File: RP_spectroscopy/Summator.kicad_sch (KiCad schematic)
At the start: 18 parts, among them U1 AD8603, U2 ADG417BR

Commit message: Almost finished the summator. Added also some components in the connectors schematic
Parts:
- added C7: 2.2µ, symbol Device:C
- added R11: 47R, symbol Device:R
- added R12, R13, R14, R15, R16, R17: 3k, symbol Device:R
- added R18: 49R9, symbol Device:R
- added R19: 1k, symbol Device:R
- added RV1: 20k, symbol Device:R_Potentiometer_Trim
- added TP1: TestPoint_Flag, symbol Connector:TestPoint_Flag
- added U3: AD8397, Package_CSP:LFCSP-8-1EP_3x3mm_P0.5mm_EP1.6x2.34mm, symbol Amplifier_Operational:ADA4610-2xCP
- C1, C2, C3, C4, C5, C6: value C -> 2.2µ
- R10: value R -> 20k
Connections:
- net GND: now also U1.2 (V-), U2.3 (GND), C7.2, R11.2, RV1.1, U3.5 (+)
- net Sweep/Fast PID: now also R11.1, R12.1, R13.1
- net at U2.8: now also R12.2, U3.3 (+)
- net at R10.2, U1.1: now also R16.1
- net at U1.3 (+): now also RV1.2, TP1.1
- net +3V3: now reaches U1.5 (V+)
- net +3V3: now also R19.1
- net +5VA: now reaches U2.4 (V+)
- net +5VA: now also U3.8 (V+)
- net -5VA: now reaches U2.7 (V-)
- net -5VA: now also U3.4 (V-), U3.9 (V-)
- new net: R13.2, R14.1, U3.2 (-)
- new net: R14.2, R15.1, U3.1
- new net: R15.2, R16.2, R17.1, U3.6 (-)
- new net: R17.2, R18.1, U3.7
- new net: C7.1, R19.2, RV1.3
- new net Summed signals: R18.2
- no-connect marks 0 -> 1
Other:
- moved on the sheet: R10

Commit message: Continued with the connection scheet
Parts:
- U1: footprint Package_TO_SOT_SMD:TSOT-23-5 -> Package_TO_SOT_SMD:TSOT-23-5_HandSoldering
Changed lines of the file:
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@@
 			)
 		)
-		(property "Footprint" "Package_TO_SOT_SMD:TSOT-23-5"
+		(property "Footprint" "Package_TO_SOT_SMD:TSOT-23-5_HandSoldering"
 			(at 160.02 128.27 0)
 			(effects

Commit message: Commit before deleting the VCO schematic from the main project. I have a separate project for that.
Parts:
- C1, C2, C3, C4, C5, C6, C7: footprint (none) -> Capacitor_SMD:C_0805_2012Metric_Pad1.18x1.45mm_HandSolder
- R1, R10, R11, R12, R13, R14, R15, R16, R17, R18, R19, R2, R3, R4, R5, R6, R7, R8, R9: footprint (none) -> Resistor_SMD:R_0805_2012Metric_Pad1.20x1.40mm_HandSolder
- RV1: footprint (none) -> Potentiometer_SMD:Potentiometer_Bourns_3224G_Horizontal
- TP1: footprint (none) -> TestPoint:TestPoint_Pad_3.0x3.0mm
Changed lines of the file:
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@@
 			)
 		)
-		(property "Footprint" ""
+		(property "Footprint" "Resistor_SMD:R_0805_2012Metric_Pad1.20x1.40mm_HandSolder"
 			(at 53.34 90.932 90)
 			(effects
@@
 			)
 		)
-		(property "Description" "Resistor"
+		(property "Description" "Resistor, 1k 1%"
 			(at 53.34 92.71 0)
 			(effects
@@
 			)
 		)
-		(property "Footprint" ""
+		(property "Footprint" "Resistor_SMD:R_0805_2012Metric_Pad1.20x1.40mm_HandSolder"
 			(at 45.212 73.66 90)
 			(effects
@@
 			)
 		)
-		(property "Description" "Resistor"
+		(property "Description" "Resistor, 47R 1%"
 			(at 46.99 73.66 0)
 			(effects
@@
 			)
 		)
-		(property "Footprint" ""
+		(property "Footprint" "Resistor_SMD:R_0805_2012Metric_Pad1.20x1.40mm_HandSolder"
 			(at 53.34 167.132 90)
 			(effects
@@
 			)
 		)
-		(property "Description" "Resistor"
+		(property "Description" "Resistor, 1k 1%"
 			(at 53.34 168.91 0)
 			(effects
@@
 			)
 		)
-		(property "Footprint" ""
+		(property "Footprint" "Resistor_SMD:R_0805_2012Metric_Pad1.20x1.40mm_HandSolder"
 			(at 53.34 129.032 90)
 			(effects
@@
 			)
 		)
-		(property "Description" "Resistor"
+		(property "Description" "Resistor, 1k 1%"
 			(at 53.34 130.81 0)
 			(effects
@@
 			)
 		)
-		(property "Footprint" ""
+		(property "Footprint" "Resistor_SMD:R_0805_2012Metric_Pad1.20x1.40mm_HandSolder"
 			(at 68.58 75.438 90)
 			(effects
@@
 			)
 		)
-		(property "Description" "Resistor"
+		(property "Description" "Resistor, 3k 1%"
 			(at 68.58 73.66 0)
 			(effects
@@
 			)
 		)
-		(property "Footprint" ""
+		(property "Footprint" "Capacitor_SMD:C_0805_2012Metric_Pad1.18x1.45mm_HandSolder"
 			(at 100.0252 106.68 0)
 			(effects
@@
 			)
 		)
-		(property "Description" "Unpolarized capacitor"
+		(property "Description" "Unpolarized capacitor, 2.2µ X7R 50V"
 			(at 99.06 102.87 0)
 			(effects
@@
 			)
 		)
-		(property "Footprint" ""
+		(property "Footprint" "Resistor_SMD:R_0805_2012Metric_Pad1.20x1.40mm_HandSolder"
 			(at 85.09 83.058 90)
 			(effects
@@
 			)
 		)
-		(property "Description" "Resistor"
+		(property "Description" "Resistor, 3k 1%"
 			(at 85.09 81.28 0)
 			(effects
@@
 			)
 		)
-		(property "Footprint" ""
+		(property "Footprint" "Resistor_SMD:R_0805_2012Metric_Pad1.20x1.40mm_HandSolder"
 			(at 83.82 167.132 90)
 			(effects
@@
 			)
 		)
-		(property "Description" "Resistor"
+		(property "Description" "Resistor, 1k 1%"
 			(at 83.82 168.91 0)
 			(effects
@@
 			)
 		)
-		(property "Footprint" ""
+		(property "Footprint" "Resistor_SMD:R_0805_2012Metric_Pad1.20x1.40mm_HandSolder"
 			(at 127 145.288 90)
 			(effects
@@
 			)
 		)
-		(property "Footprint" ""
+		(property "Footprint" "Resistor_SMD:R_0805_2012Metric_Pad1.20x1.40mm_HandSolder"
 			(at 127 119.888 90)
 			(effects
@@
 			)
 		)
-		(property "Footprint" ""
+		(property "Footprint" "Capacitor_SMD:C_0805_2012Metric_Pad1.18x1.45mm_HandSolder"
 			(at 69.5452 106.68 0)
 			(effects
@@
 			)
 		)
-		(property "Description" "Unpolarized capacitor"
+		(property "Description" "Unpolarized capacitor, 2.2µ X7R 50V"
 			(at 68.58 102.87 0)
 			(effects
@@
 			)
 		)
-		(property "Footprint" ""
+		(property "Footprint" "Resistor_SMD:R_0805_2012Metric_Pad1.20x1.40mm_HandSolder"
 			(at 83.82 90.932 90)
 			(effects
@@
 			)
 		)
-		(property "Description" "Resistor"
+		(property "Description" "Resistor, 1k 1%"
 			(at 83.82 92.71 0)
 			(effects
@@
 			)
 		)
-		(property "Footprint" ""
+		(property "Footprint" "Resistor_SMD:R_0805_2012Metric_Pad1.20x1.40mm_HandSolder"
 			(at 160.02 152.908 90)
 			(effects
@@
 			)
 		)
-		(property "Description" "Resistor"
+		(property "Description" "Resistor, 20k 1%"
 			(at 160.02 151.13 0)
 			(effects
@@
 			)
 		)
-		(property "Footprint" ""
+		(property "Footprint" "Resistor_SMD:R_0805_2012Metric_Pad1.20x1.40mm_HandSolder"
 			(at 68.58 62.738 90)
 			(effects
@@
 			)
 		)
-		(property "Description" "Resistor"
+		(property "Description" "Resistor, 3k 1%"
 			(at 68.58 60.96 0)
 			(effects
@@
 			)
 		)
-		(property "Footprint" ""
+		(property "Footprint" "Capacitor_SMD:C_0805_2012Metric_Pad1.18x1.45mm_HandSolder"
 			(at 69.5452 144.78 0)
 			(effects
@@
 			)
 		)
-		(property "Description" "Unpolarized capacitor"
+		(property "Description" "Unpolarized capacitor, 2.2µ X7R 50V"
 			(at 68.58 140.97 0)
 			(effects
@@
 			)
 		)
-		(property "Footprint" ""
+		(property "Footprint" "Capacitor_SMD:C_0805_2012Metric_Pad1.18x1.45mm_HandSolder"
 			(at 100.0252 144.78 0)
 			(effects
@@
 			)
 		)
-		(property "Description" "Unpolarized capacitor"
+		(property "Description" "Unpolarized capacitor, 2.2µ X7R 50V"
 			(at 99.06 140.97 0)
 			(effects
@@
 			)
 		)
-		(property "Footprint" ""
+		(property "Footprint" "Resistor_SMD:R_0805_2012Metric_Pad1.20x1.40mm_HandSolder"
 			(at 187.96 102.108 90)
 			(effects
@@
 			)
 		)
-		(property "Description" "Resistor"
+		(property "Description" "Resistor, 3k 1%"
 			(at 187.96 100.33 0)
 			(effects
@@
 			)
 		)
-		(property "Footprint" ""
+		(property "Footprint" "Resistor_SMD:R_0805_2012Metric_Pad1.20x1.40mm_HandSolder"
 			(at 127 132.588 90)
 			(effects
@@
 			)
 		)
-		(property "Footprint" ""
+		(property "Footprint" "Resistor_SMD:R_0805_2012Metric_Pad1.20x1.40mm_HandSolder"
 			(at 233.68 93.218 90)
 			(effects
@@
 			)
 		)
-		(property "Description" "Resistor"
+		(property "Description" "Resistor, 49R9 1%"
 			(at 233.68 91.44 0)
 			(effects
@@
 			)
 		)
-		(property "Footprint" ""
+		(property "Footprint" "Capacitor_SMD:C_0805_2012Metric_Pad1.18x1.45mm_HandSolder"
 			(at 69.5452 182.88 0)
 			(effects
@@
 			)
 		)
-		(property "Description" "Unpolarized capacitor"
+		(property "Description" "Unpolarized capacitor, 2.2µ X7R 50V"
 			(at 68.58 179.07 0)
 			(effects
@@
 			)
 		)
-		(property "Footprint" ""
+		(property "Footprint" "Capacitor_SMD:C_0805_2012Metric_Pad1.18x1.45mm_HandSolder"
 			(at 100.0252 182.88 0)
 			(effects
@@
 			)
 		)
-		(property "Description" "Unpolarized capacitor"
+		(property "Description" "Unpolarized capacitor, 2.2µ X7R 50V"
 			(at 99.06 179.07 0)
 			(effects
@@
 			)
 		)
-		(property "Footprint" ""
+		(property "Footprint" "TestPoint:TestPoint_Pad_3.0x3.0mm"
 			(at 135.89 99.06 0)
 			(effects
@@
 			)
 		)
-		(property "Footprint" ""
+		(property "Footprint" "Potentiometer_SMD:Potentiometer_Bourns_3224G_Horizontal"
 			(at 152.4 99.06 0)
 			(effects
@@
 			)
 		)
-		(property "Description" "Trim-potentiometer"
+		(property "Description" "Trim-potentiometer, 20k"
 			(at 152.4 99.06 0)
 			(effects
@@
 			)
 		)
-		(property "Footprint" ""
+		(property "Footprint" "Resistor_SMD:R_0805_2012Metric_Pad1.20x1.40mm_HandSolder"
 			(at 214.63 109.728 90)
 			(effects
@@
 			)
 		)
-		(property "Description" "Resistor"
+		(property "Description" "Resistor, 3k 1%"
 			(at 214.63 107.95 0)
 			(effects
@@
 			)
 		)
-		(property "Footprint" ""
+		(property "Footprint" "Capacitor_SMD:C_0805_2012Metric_Pad1.18x1.45mm_HandSolder"
 			(at 166.0652 102.87 0)
 			(effects
@@
 			)
 		)
-		(property "Description" "Unpolarized capacitor"
+		(property "Description" "Unpolarized capacitor, 2.2µ X7R 50V"
 			(at 165.1 99.06 0)
 			(effects
@@
 			)
 		)
-		(property "Footprint" ""
+		(property "Footprint" "Resistor_SMD:R_0805_2012Metric_Pad1.20x1.40mm_HandSolder"
 			(at 83.82 129.032 90)
 			(effects
@@
 			)
 		)
-		(property "Description" "Resistor"
+		(property "Description" "Resistor, 1k 1%"
 			(at 83.82 130.81 0)
 			(effects
@@
 			)
 		)
-		(property "Footprint" ""
+		(property "Footprint" "Resistor_SMD:R_0805_2012Metric_Pad1.20x1.40mm_HandSolder"
 			(at 150.622 88.9 90)
 			(effects
@@
 			)
 		)
-		(property "Description" "Resistor"
+		(property "Description" "Resistor, 1k 1%"
 			(at 152.4 88.9 0)
 			(effects
@@
 			)
 		)
-		(property "Footprint" ""
+		(property "Footprint" "Resistor_SMD:R_0805_2012Metric_Pad1.20x1.40mm_HandSolder"
 			(at 187.96 89.408 90)
 			(effects
@@
 			)
 		)
-		(property "Description" "Resistor"
+		(property "Description" "Resistor, 3k 1%"
 			(at 187.96 87.63 0)
 			(effects

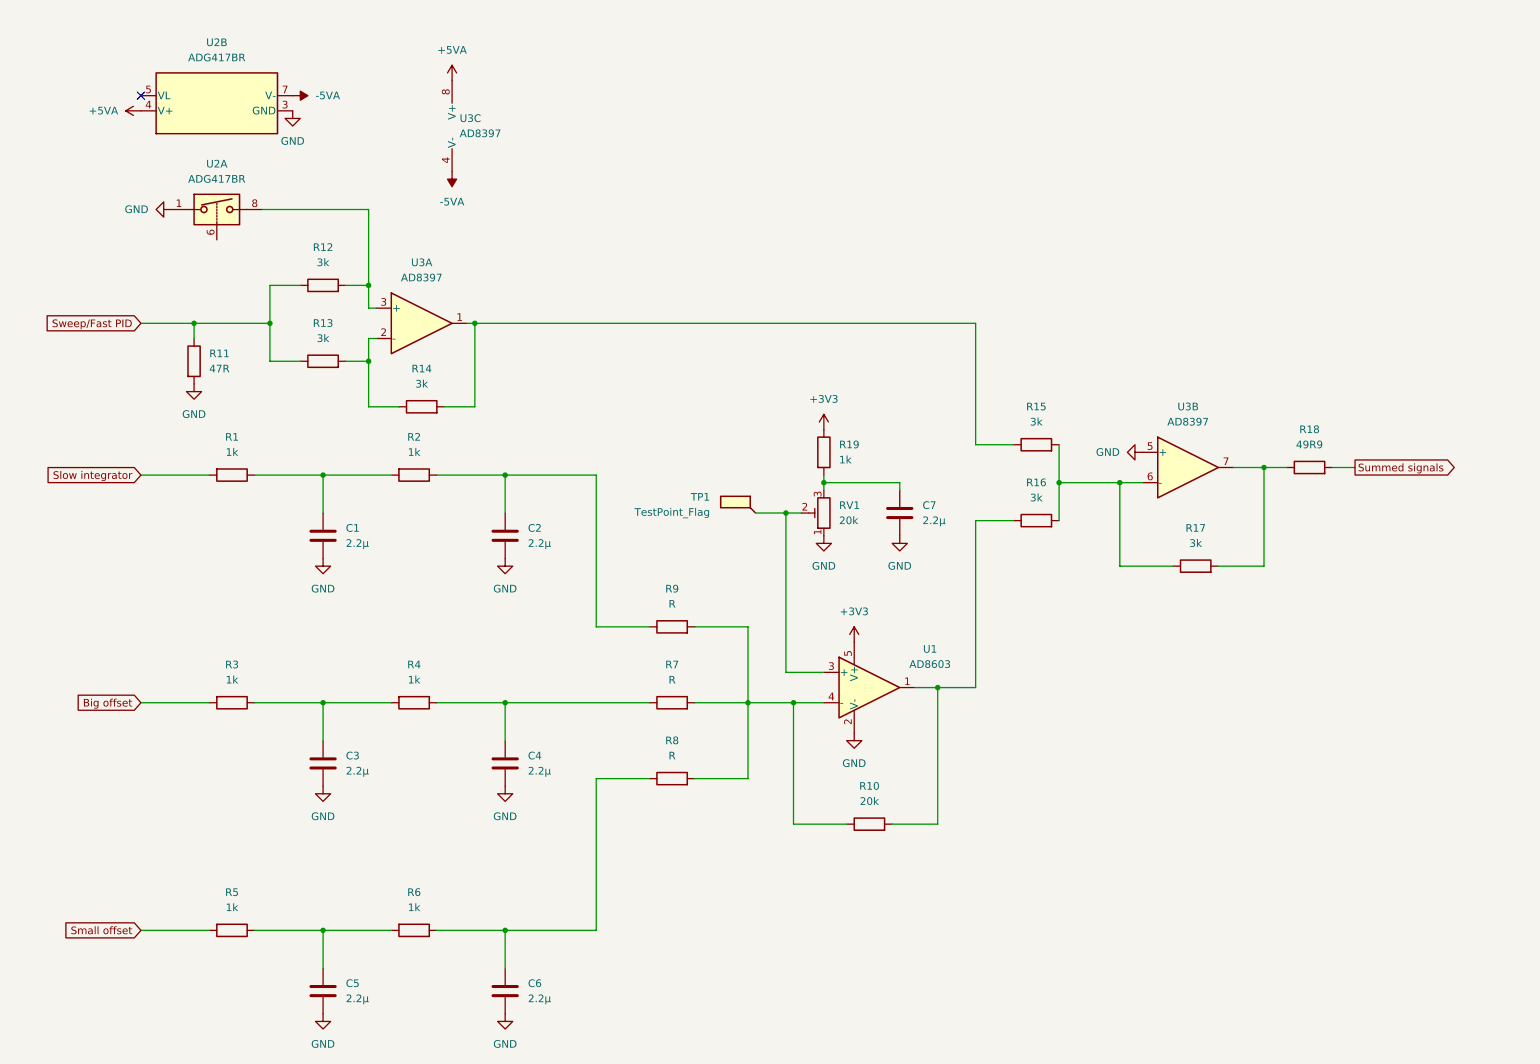
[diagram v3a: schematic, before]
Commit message: Added the EMI filter in the +5V branch and added the powerline capacitors for the remaining opamps. Removed the tunable offset from the summator. Assigned right footprints and specs to all the components.
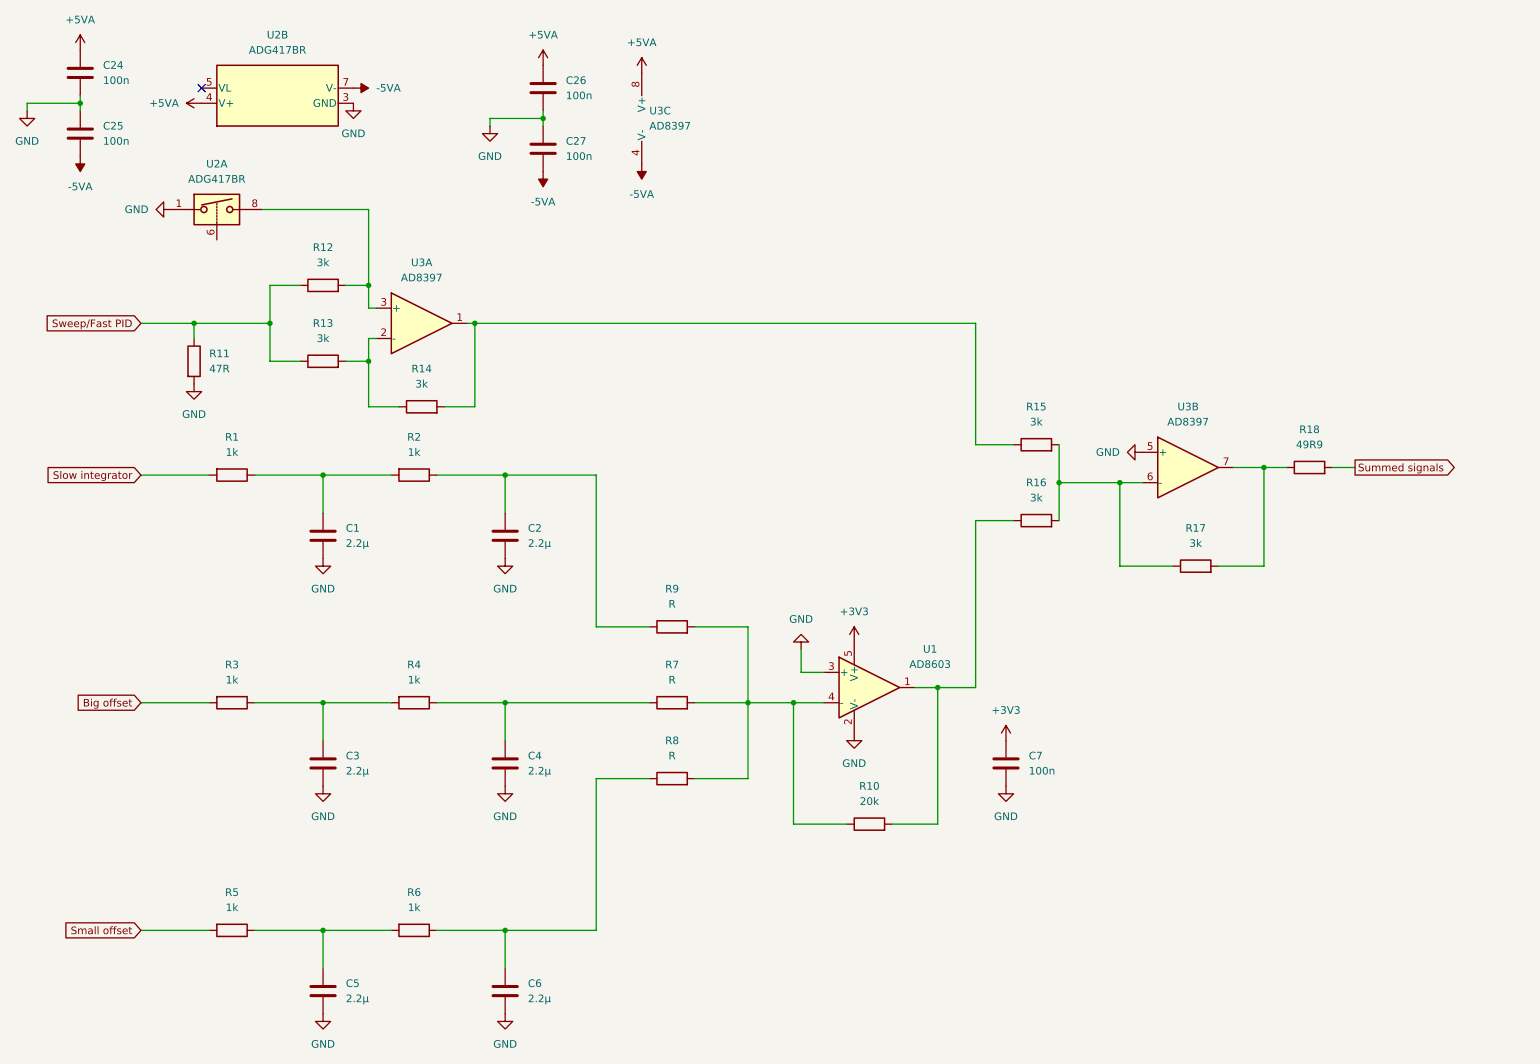
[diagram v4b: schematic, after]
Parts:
- removed R19: 1k, Resistor_SMD:R_0805_2012Metric_Pad1.20x1.40mm_HandSolder, symbol Device:R
- removed RV1: 20k, Potentiometer_SMD:Potentiometer_Bourns_3224G_Horizontal, symbol Device:R_Potentiometer_Trim
- removed TP1: TestPoint_Flag, TestPoint:TestPoint_Pad_3.0x3.0mm, symbol Connector:TestPoint_Flag
- added C24, C25, C26, C27: 100n, Capacitor_SMD:C_0805_2012Metric_Pad1.18x1.45mm_HandSolder, symbol Device:C
- C7: value 2.2µ -> 100n
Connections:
- net +3V3: now also C7.1
- net +5VA: now also C24.1, C26.1
- net -5VA: now also C25.2, C27.2
- net GND: now also U1.3 (+), C24.2, C25.1, C26.2, C27.1
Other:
- moved on the sheet: U2B, U3C

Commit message: Changed the way of implementing the powerline capacitors in order to find them easily while creating the pcb. Started implementing the double Sallen-Key filter.
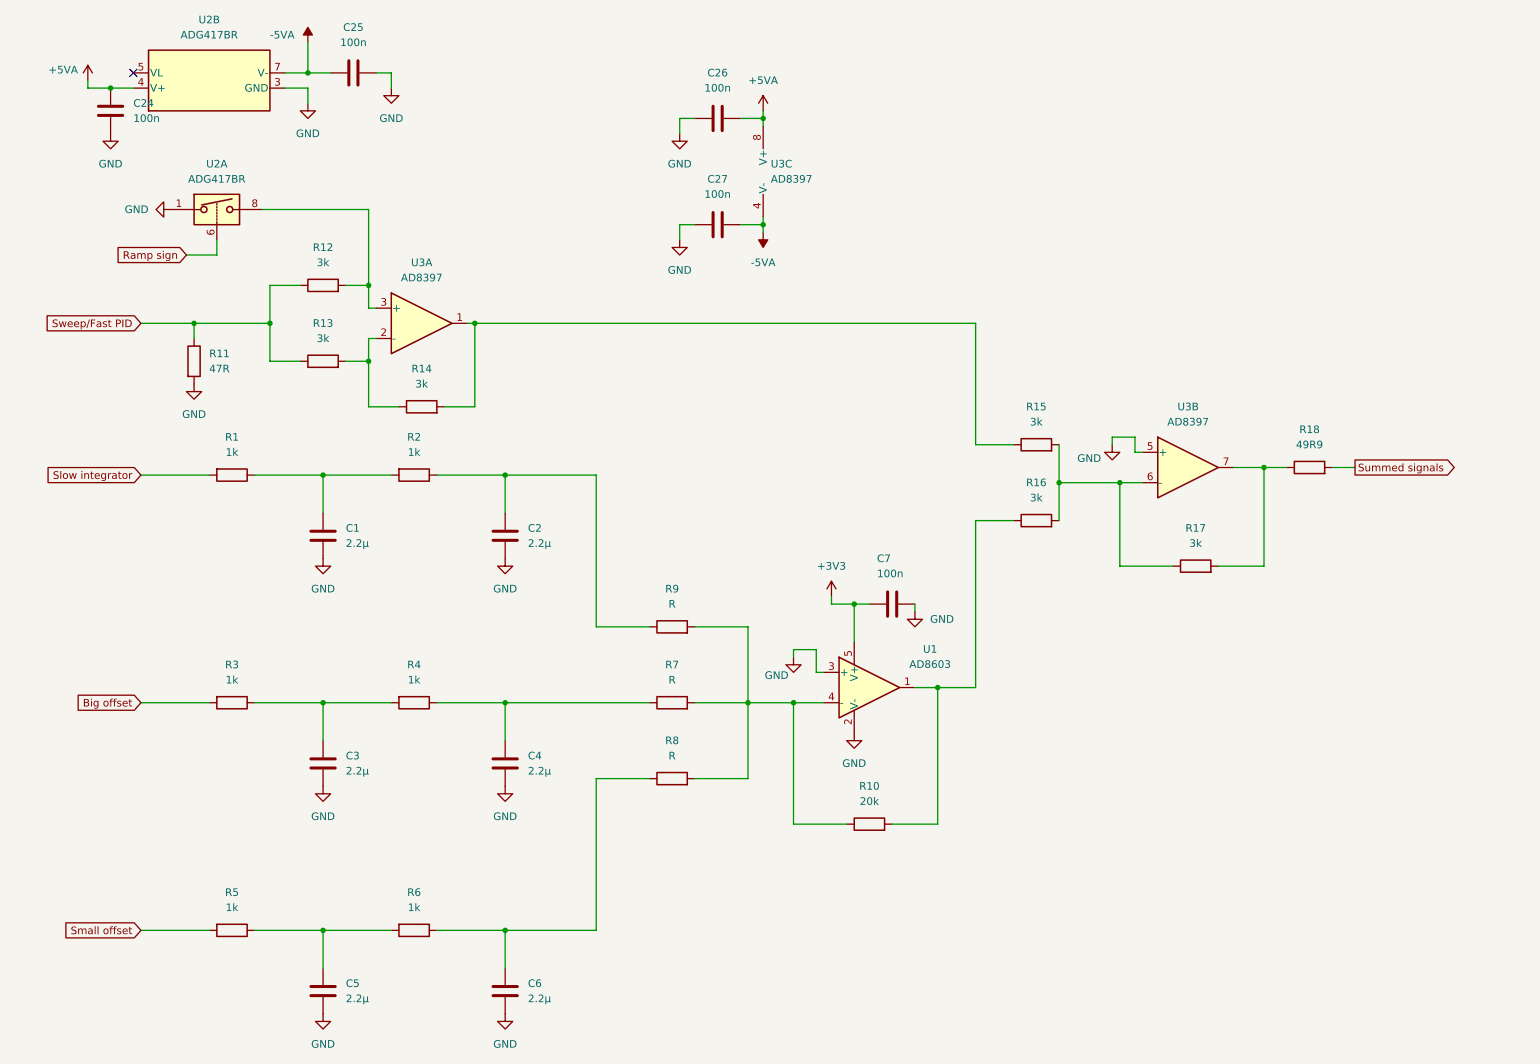
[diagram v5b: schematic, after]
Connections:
- net +5VA: now also C26.2; no longer C26.1
- net -5VA: now also C25.1; no longer C25.2
- net GND: now also C25.2, C26.1; no longer C25.1, C26.2
- net Ramp sign: now reaches U2.6
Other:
- moved on the sheet: C24, C25, C26, C27, C7, U2B, U3C

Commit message: Started to place all the components on the PCB. Simulated a bunch of filters.
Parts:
- U1: footprint Package_TO_SOT_SMD:TSOT-23-5_HandSoldering -> Package_SO:SOIC-8_3.9x4.9mm_P1.27mm
- U3: footprint Package_CSP:LFCSP-8-1EP_3x3mm_P0.5mm_EP1.6x2.34mm -> Package_SO:SOIC-8_3.9x4.9mm_P1.27mm
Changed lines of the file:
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@@
 			)
 		)
-		(property "Footprint" "Package_CSP:LFCSP-8-1EP_3x3mm_P0.5mm_EP1.6x2.34mm"
+		(property "Footprint" "Package_SO:SOIC-8_3.9x4.9mm_P1.27mm"
 			(at 85.09 67.31 0)
 			(effects
@@
 			)
 		)
-		(property "Footprint" "Package_TO_SOT_SMD:TSOT-23-5_HandSoldering"
+		(property "Footprint" "Package_SO:SOIC-8_3.9x4.9mm_P1.27mm"
 			(at 160.02 128.27 0)
 			(effects
@@
 			)
 		)
-		(property "Footprint" "Package_CSP:LFCSP-8-1EP_3x3mm_P0.5mm_EP1.6x2.34mm"
+		(property "Footprint" "Package_SO:SOIC-8_3.9x4.9mm_P1.27mm"
 			(at 213.36 91.44 0)
 			(effects
@@
 			)
 		)
-		(property "Footprint" "Package_CSP:LFCSP-8-1EP_3x3mm_P0.5mm_EP1.6x2.34mm"
+		(property "Footprint" "Package_SO:SOIC-8_3.9x4.9mm_P1.27mm"
 			(at 144.78 41.91 0)
 			(effects
